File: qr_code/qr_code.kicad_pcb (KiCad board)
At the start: 2 copper layers, 86.6 x 60.5 mm, 89 parts, among them J10 DG141R-04, J2 Prog (PinHeader_2x03_P2.54mm), J3 Debbag GPIO (PinHeader_01x02_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, J7 Usart_debbag (PinHeader_1x04_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, J8 Usart_debbag (PinHeader_1x04_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, J9 DG141R-04, Q1 DTC114ECA (SOT-23), Q2 DTC114ECA (SOT-23), U1 PAI141M30 (SOIC-16), U2 ADM3485EARZ-REEL (SOIC-8)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

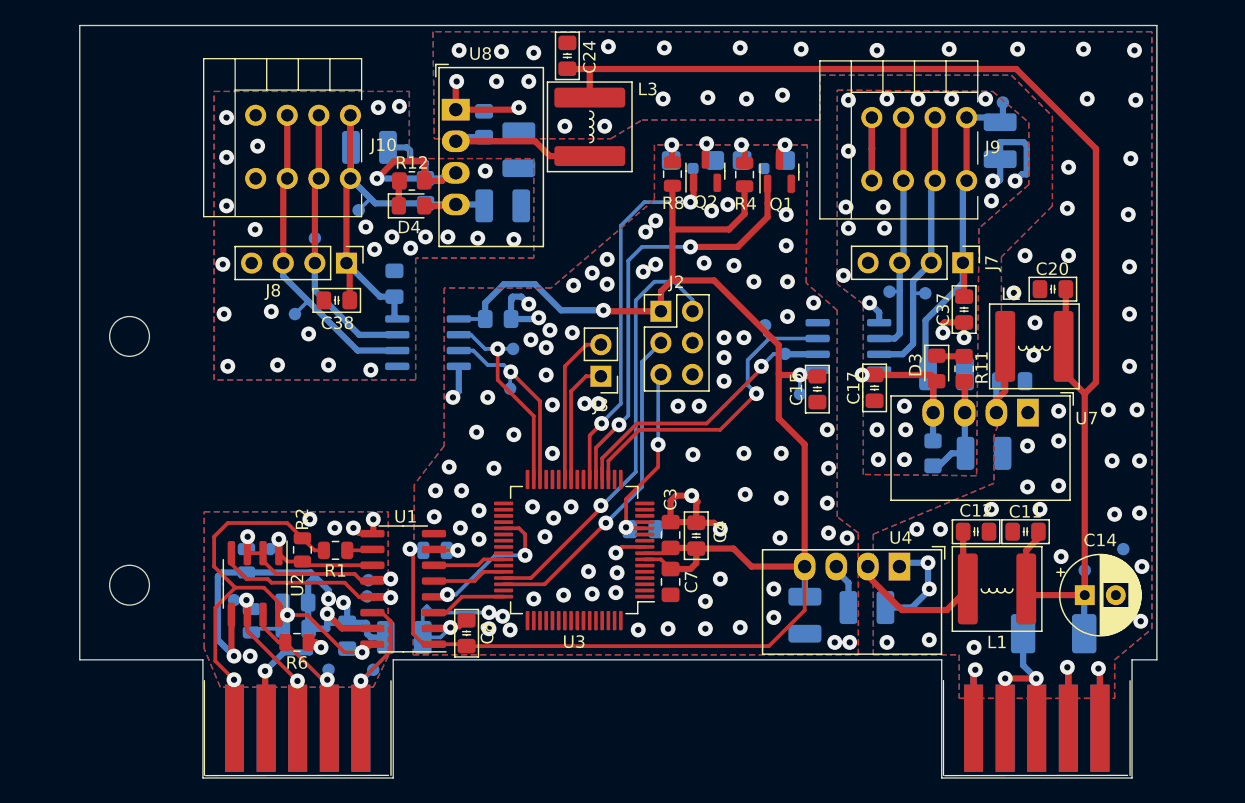
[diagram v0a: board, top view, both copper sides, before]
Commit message: all замменил резисторы failsafe в плате контроллера и обрал из перечня во всех остальных
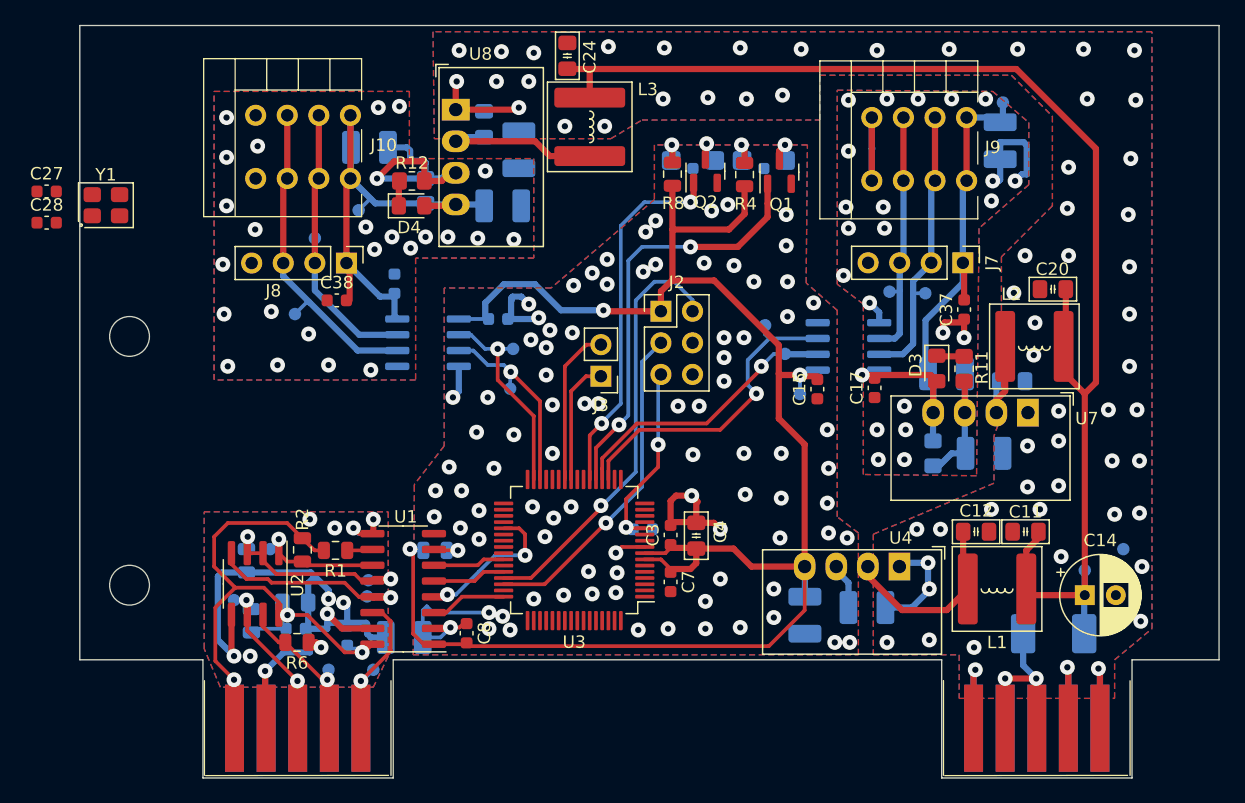
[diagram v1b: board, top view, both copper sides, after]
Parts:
- added C27: 20pF 50V 0603, Capacitor_SMD:C_0603_1608Metric, F.Cu at (62.3, 102.8)
- added C28: 20pF 50V 0603, Capacitor_SMD:C_0603_1608Metric, F.Cu at (62.3, 105.4)
- added Y1: Crystal_3225 8MHz, PCM_Crystal_AKL:Crystal_SMD_3225-4Pin_3.2x2.5mm, F.Cu at (67.1, 104.0)
- C15, C16, C17, C18, C37, C38, C5, C8, C9: value 0,1uF 100V 0805 -> 0,1uF 100V 0603; footprint PCM_Capacitor_SMD_AKL:C_0805_2012Metric_Pad1.18x1.45mm_HandSolder -> Capacitor_SMD:C_0603_1608Metric
- C3, C6, C7: value 0,1uF 100V 0805 -> 0,1uF 100V 0603; footprint Capacitor_SMD:C_0805_2012Metric_Pad1.18x1.45mm_HandSolder -> Capacitor_SMD:C_0603_1608Metric
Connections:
- U3 pad 10: unconnected-(U3-PF0-Pad10) -> /OSC_IN
- U3 pad 11: unconnected-(U3-PF1-Pad11) -> /OSC_OUT
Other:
- board size 86.6 x 60.5 mm -> 91.6 x 60.5 mm

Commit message: QRcode udate size and schems
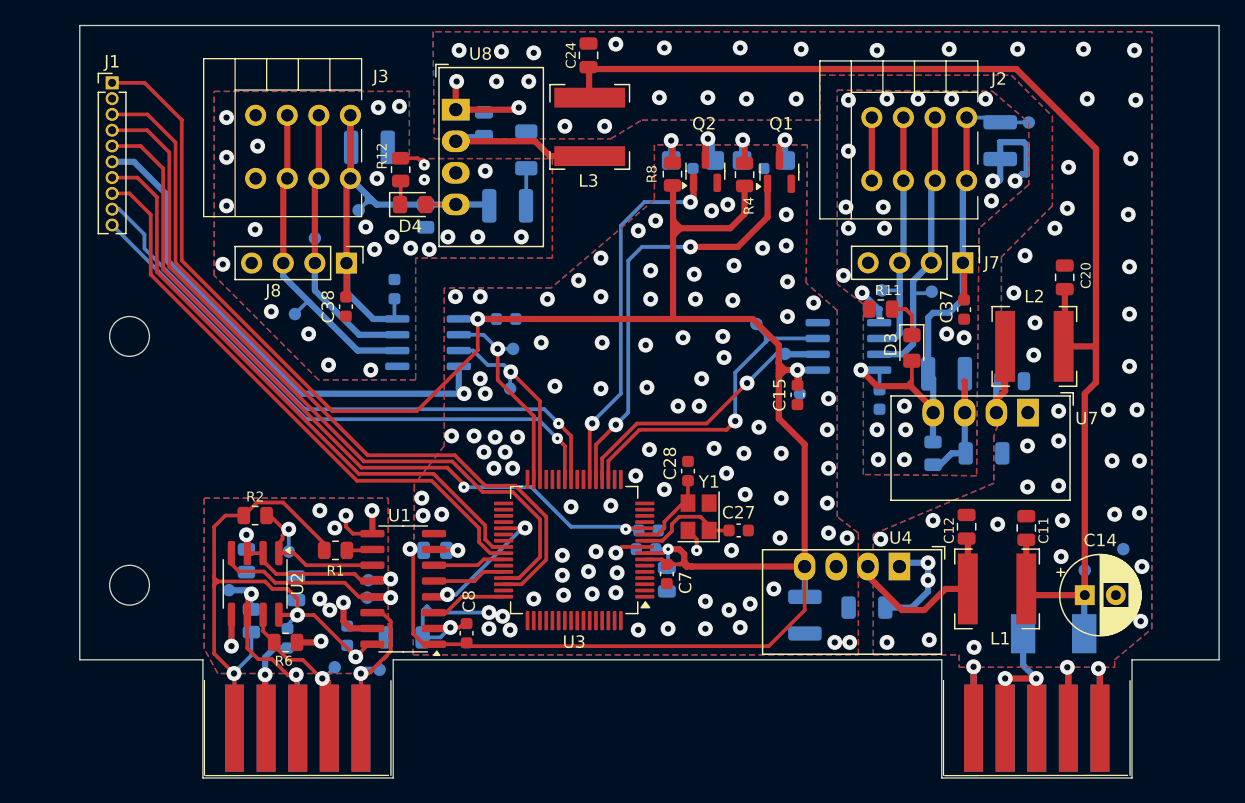
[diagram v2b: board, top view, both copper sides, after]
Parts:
- removed J10, J9: DG141R-04, Connector:DG141R-04
- added G***: LOGO, Symbol:PB_LOGO, B.Cu at (146.1, 98.0)
- added J1: PLL-10 (Prog), Connector_PinHeader_1.27mm:PinHeader_1x10_P1.27mm_Vertical, F.Cu at (67.6, 94.1)
- C1, C11, C12, C20, C21, C24, C25: footprint PCM_Capacitor_SMD_AKL:C_0805_2012Metric_Pad1.18x1.45mm_HandSolder -> Capacitor_SMD:C_0805_2012Metric
- C10, C19, C23, C35, C36: footprint PCM_Capacitor_SMD_AKL:C_1210_3225Metric_Pad1.42x2.65mm_HandSolder -> Capacitor_SMD:C_1210_3225Metric
- C13, C2, C22, C26: footprint PCM_Capacitor_SMD_Handsoldering_AKL:C_1210_3225Metric_Pad1.42x2.65mm -> Capacitor_SMD:C_1206_3216Metric
- C14: footprint PCM_Capacitor_THT_AKL:CP_Radial_D6.3mm_P2.50mm -> Capacitor_THT:CP_Radial_D6.3mm_P2.50mm
- C17, C3: moved to B.Cu
- C4: footprint PCM_Capacitor_SMD_AKL:C_0805_2012Metric_Pad1.18x1.45mm_HandSolder -> Capacitor_SMD:C_0805_2012Metric; moved to B.Cu
- F1: footprint PCM_Fuse_Handsoldering_AKL:Fuse_Littelfuse-NANO2-451_453 -> Fuse:Fuse_Littelfuse-NANO2-451_453
- J2: value Prog (PinHeader_2x03_P2.54mm) -> DG141R-04; footprint Connector_PinHeader_2.54mm:PinHeader_2x03_P2.54mm_Vertical -> Connector:DG141R-04
- J3: value Debbag GPIO (PinHeader_01x02_P2.54mm) -> DG141R-04; footprint Connector_PinHeader_2.54mm:PinHeader_1x02_P2.54mm_Vertical -> Connector:DG141R-04
- L1, L2, L3: footprint PCM_Inductor_SMD_Handsoldering_AKL:L_Bourns-SRN6028 -> Inductor_SMD:L_Bourns-SRN6028
- R1, R2, R3, R4, R5, R6, R7, R8: footprint PCM_4ms_Resistor:R_0805_2012Metric -> Resistor_SMD:R_0805_2012Metric
- R10, R11, R12, R9: footprint Resistor_SMD:R_0805_2012Metric_Pad1.20x1.40mm_HandSolder -> Resistor_SMD:R_0805_2012Metric
- TP1, TP10, TP11, TP12, TP13, TP14, TP15, TP16, TP17, TP18, TP19, TP2, TP3, TP4, TP5, TP6, TP7, TP8, TP9: footprint PCM_4ms_TestPoint:TestPoint_D1 -> TestPoint:TestPoint_Pad_D1.0mm
- Y1: footprint PCM_Crystal_AKL:Crystal_SMD_3225-4Pin_3.2x2.5mm -> Crystal:Crystal_SMD_3225-4Pin_3.2x2.5mm
- moved C27 62.0 mm to (118.0, 130.1)
- moved C28 55.3 mm to (113.9, 125.3), turned to 90 degrees
- moved Y1 53.8 mm to (114.8, 129.0), turned to 90 degrees
- moved J2 31.8 mm to (141.0, 99.9), turned to -90 degrees
- moved J3 23.7 mm to (91.5, 99.8), turned to -90 degrees
- moved R11 8.24 mm to (129.4, 112.3), turned to 0 degrees
- moved R2 4.70 mm to (79.1, 128.9), turned to 180 degrees
- moved C4 4.25 mm to (112.2, 134.1), turned to -90 degrees
- moved TP10 2.63 mm to (141.3, 97.3)
- moved D3 2.59 mm to (131.9, 115.4)
- moved C3 2.28 mm to (110.5, 131.6), turned to 180 degrees
- moved R10 2.01 mm to (92.8, 104.8), turned to 90 degrees
- moved C24 1.70 mm to (105.9, 91.9)
- moved C15 1.67 mm to (122.7, 119.2)
- moved TP2 1.51 mm to (81.8, 131.8)
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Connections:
- J2 pad 1: +3V3 -> /Vcc_1
- J2 pad 2: /SWDIO -> /RX_1
- J2 pad 3: /SWCLK -> /TX_1
- J2 pad 4: unconnected-(J2-Pin_4-Pad4) -> /GND_1
- J3 pad 1: /GPIO1 -> /Vcc_2
- J3 pad 2: /GPIO2 -> /RX_2
- U3 pad 39: /UART_DE -> unconnected-(U3-PC7-Pad39)
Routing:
- net +3V3: track 140.3 -> 195.0 mm, vias 3 -> 4
- net /UART_TX: track 0.00 -> 48.0 mm
- net /UART_RX: track 0.00 -> 46.9 mm
- net /NRST: track 15.0 -> 61.7 mm
- net /GPIO1: track 10.00 -> 48.6 mm, vias 0 -> 1
- net /SWCLK: track 26.6 -> 61.7 mm, vias 1 -> 0
- net /GPIO2: track 12.7 -> 46.5 mm, vias 0 -> 1
- net GND1: track 59.5 -> 26.3 mm, vias 11 -> 10
- net /SWDIO: track 34.8 -> 59.4 mm, vias 1 -> 0
- net GNDD: track 38.7 -> 59.2 mm, vias 86 -> 94
- net /GND_2: track 20.5 -> 5.83 mm, vias 25 -> 24
- net /+3.3VRS485: track 51.9 -> 60.7 mm
- net /OSC_IN: track 0.00 -> 8.60 mm
- net /GND_1: track 37.6 -> 30.0 mm
- net Net-(RS1-Pin_3): track 13.9 -> 20.9 mm
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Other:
- board text added: "t06v02a"

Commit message: update schemas
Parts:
- removed TP9: TestPoint, TestPoint:TestPoint_Pad_D1.0mm
- added G1: TestPoint, TestPoint:TestPoint_Pad_D1.0mm, B.Cu at (85.6, 132.8)
- added GA1: TestPoint, TestPoint:TestPoint_Pad_D1.0mm, B.Cu at (141.6, 133.1)
- added GD1: TestPoint, TestPoint:TestPoint_Pad_D1.0mm, B.Cu at (119.4, 133.7)
- F1: value 0452.500MRL -> 0451.500MRL
- moved G*** 8.97 mm to (153.1, 92.4)
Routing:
- net Net-(RS2-Pin_2): track 22.6 -> 24.6 mm
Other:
- board text added: "PizzaBot inc."
